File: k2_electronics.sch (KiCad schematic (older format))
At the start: 60 parts, among them J1 Conn_ARM_JTAG_SWD_10, SW1 SW_SPST, SW10 SW_SPST, SW11 SW_SPST, SW12 SW_SPST, SW13 SW_SPST, SW14 SW_SPST, SW15 SW_SPST, SW16 SW_SPST, SW17 SW_SPST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

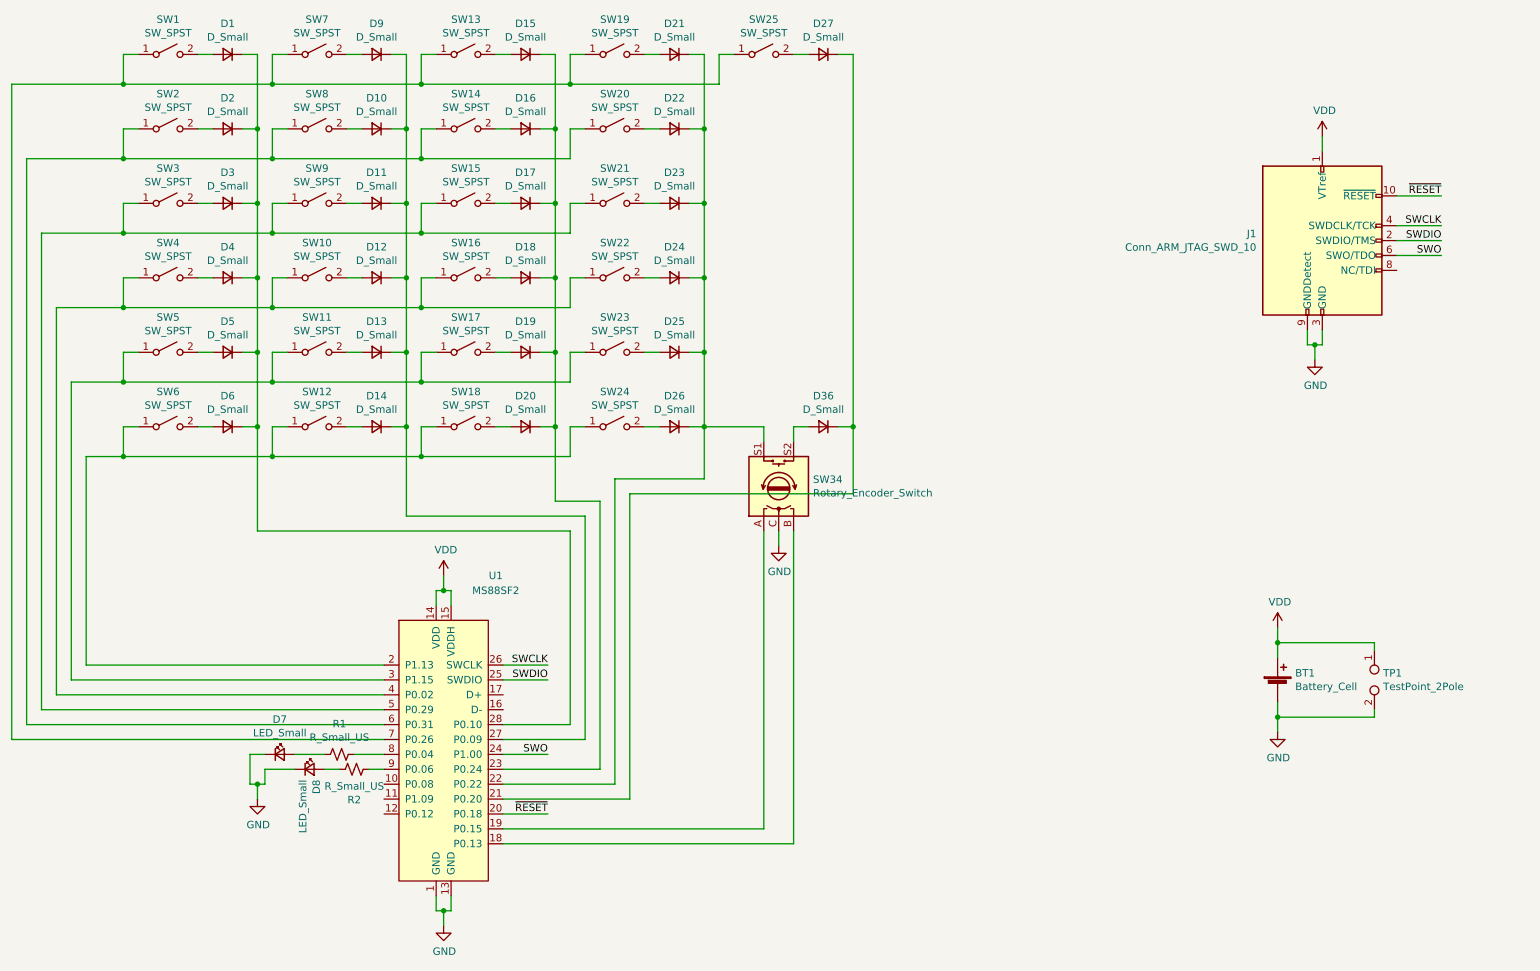
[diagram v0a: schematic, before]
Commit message: Component placement and autoroute
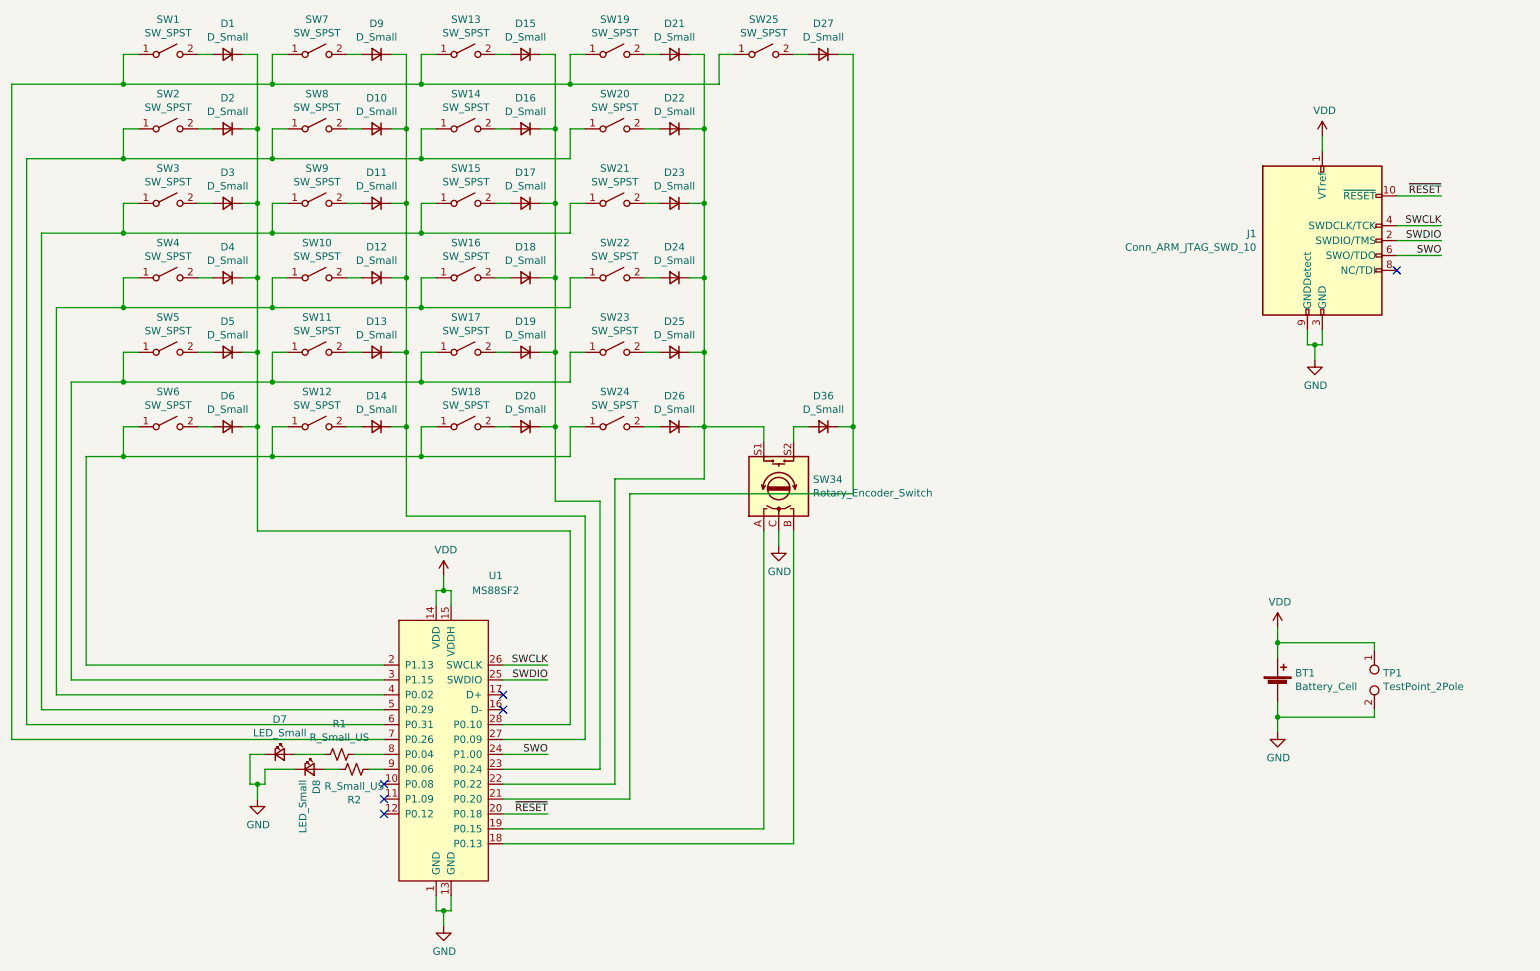
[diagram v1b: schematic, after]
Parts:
- D7, D8: footprint LED_SMD:LED_0603_1608Metric_Pad1.05x0.95mm_HandSolder -> k2:LED_0603_1608Metric_Pad1.05x0.95mm_HandSolder_reversible
- J1: footprint (none) -> Connector_PinHeader_1.27mm:PinHeader_2x05_P1.27mm_Vertical
- R1, R2: footprint Resistor_SMD:R_0603_1608Metric_Pad0.98x0.95mm_HandSolder -> k2:R_0603_1608Metric_Pad0.98x0.95mm_HandSolder_reversible
- TP1: footprint TestPoint:TestPoint_2Pads_Pitch5.08mm_Drill1.3mm -> TestPoint:TestPoint_2Pads_Pitch2.54mm_Drill0.8mm
- U1: footprint (none) -> k2:MS88F2_reversible
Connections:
- no-connect marks 0 -> 6
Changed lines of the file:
@@
 F 0 "U1" H 4150 6650 50  0000 C CNN
 F 1 "MS88SF2" H 4150 6550 50  0000 C CNN
-F 2 "" H 3800 6900 50  0001 C CNN
+F 2 "k2:MS88F2_reversible" H 3800 6900 50  0001 C CNN
 F 3 "" H 3800 6900 50  0001 C CNN
 	1    3800 5600
@@
 F 0 "D8" V 2946 5780 50  0000 R CNN
 F 1 "LED_Small" V 2855 5780 50  0000 R CNN
-F 2 "LED_SMD:LED_0603_1608Metric_Pad1.05x0.95mm_HandSolder" V 2900 5850 50  0001 C CNN
+F 2 "k2:LED_0603_1608Metric_Pad1.05x0.95mm_HandSolder_reversible" V 2900 5850 50  0001 C CNN
 F 3 "~" V 2900 5850 50  0001 C CNN
 	1    2900 5850
@@
 F 0 "D7" H 2700 5985 50  0000 C CNN
 F 1 "LED_Small" H 2700 5894 50  0000 C CNN
-F 2 "LED_SMD:LED_0603_1608Metric_Pad1.05x0.95mm_HandSolder" V 2700 5750 50  0001 C CNN
+F 2 "k2:LED_0603_1608Metric_Pad1.05x0.95mm_HandSolder_reversible" V 2700 5750 50  0001 C CNN
 F 3 "~" V 2700 5750 50  0001 C CNN
 	1    2700 5750
@@
 F 0 "R1" V 3305 5750 50  0000 C CNN
 F 1 "R_Small_US" V 3214 5750 50  0000 C CNN
-F 2 "Resistor_SMD:R_0603_1608Metric_Pad0.98x0.95mm_HandSolder" H 3100 5750 50  0001 C CNN
+F 2 "k2:R_0603_1608Metric_Pad0.98x0.95mm_HandSolder_reversible" H 3100 5750 50  0001 C CNN
 F 3 "~" H 3100 5750 50  0001 C CNN
 	1    3100 5750
@@
 F 0 "R2" V 3405 5850 50  0000 C CNN
 F 1 "R_Small_US" V 3314 5850 50  0000 C CNN
-F 2 "Resistor_SMD:R_0603_1608Metric_Pad0.98x0.95mm_HandSolder" H 3200 5850 50  0001 C CNN
+F 2 "k2:R_0603_1608Metric_Pad0.98x0.95mm_HandSolder_reversible" H 3200 5850 50  0001 C CNN
 F 3 "~" H 3200 5850 50  0001 C CNN
 	1    3200 5850
@@
 F 0 "J1" H 9257 2346 50  0000 R CNN
 F 1 "Conn_ARM_JTAG_SWD_10" H 9257 2255 50  0000 R CNN
-F 2 "" H 9700 2300 50  0001 C CNN
+F 2 "Connector_PinHeader_1.27mm:PinHeader_2x05_P1.27mm_Vertical" H 9700 2300 50  0001 C CNN
 F 3 "http://infocenter.arm.com/help/topic/com.arm.doc.ddi0314h/DDI0314H_coresight_components_trm.pdf" V 9350 1050 50  0001 C CNN
 	1    9700 2300
@@
 F 0 "TP1" V 10004 5308 50  0000 L CNN
 F 1 "TestPoint_2Pole" V 10095 5308 50  0000 L CNN
-F 2 "TestPoint:TestPoint_2Pads_Pitch5.08mm_Drill1.3mm" H 10050 5250 50  0001 C CNN
+F 2 "TestPoint:TestPoint_2Pads_Pitch2.54mm_Drill0.8mm" H 10050 5250 50  0001 C CNN
 F 3 "~" H 10050 5250 50  0001 C CNN
 	1    10050 5250
@@
 Wire Wire Line
 	6150 6350 6150 4250
+NoConn ~ 10200 2500
+NoConn ~ 3400 5950
+NoConn ~ 3400 6050
+NoConn ~ 3400 6150
+NoConn ~ 4200 5350
+NoConn ~ 4200 5450
 $EndSCHEMATC

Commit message: Ensure all footprints reversible and touchup
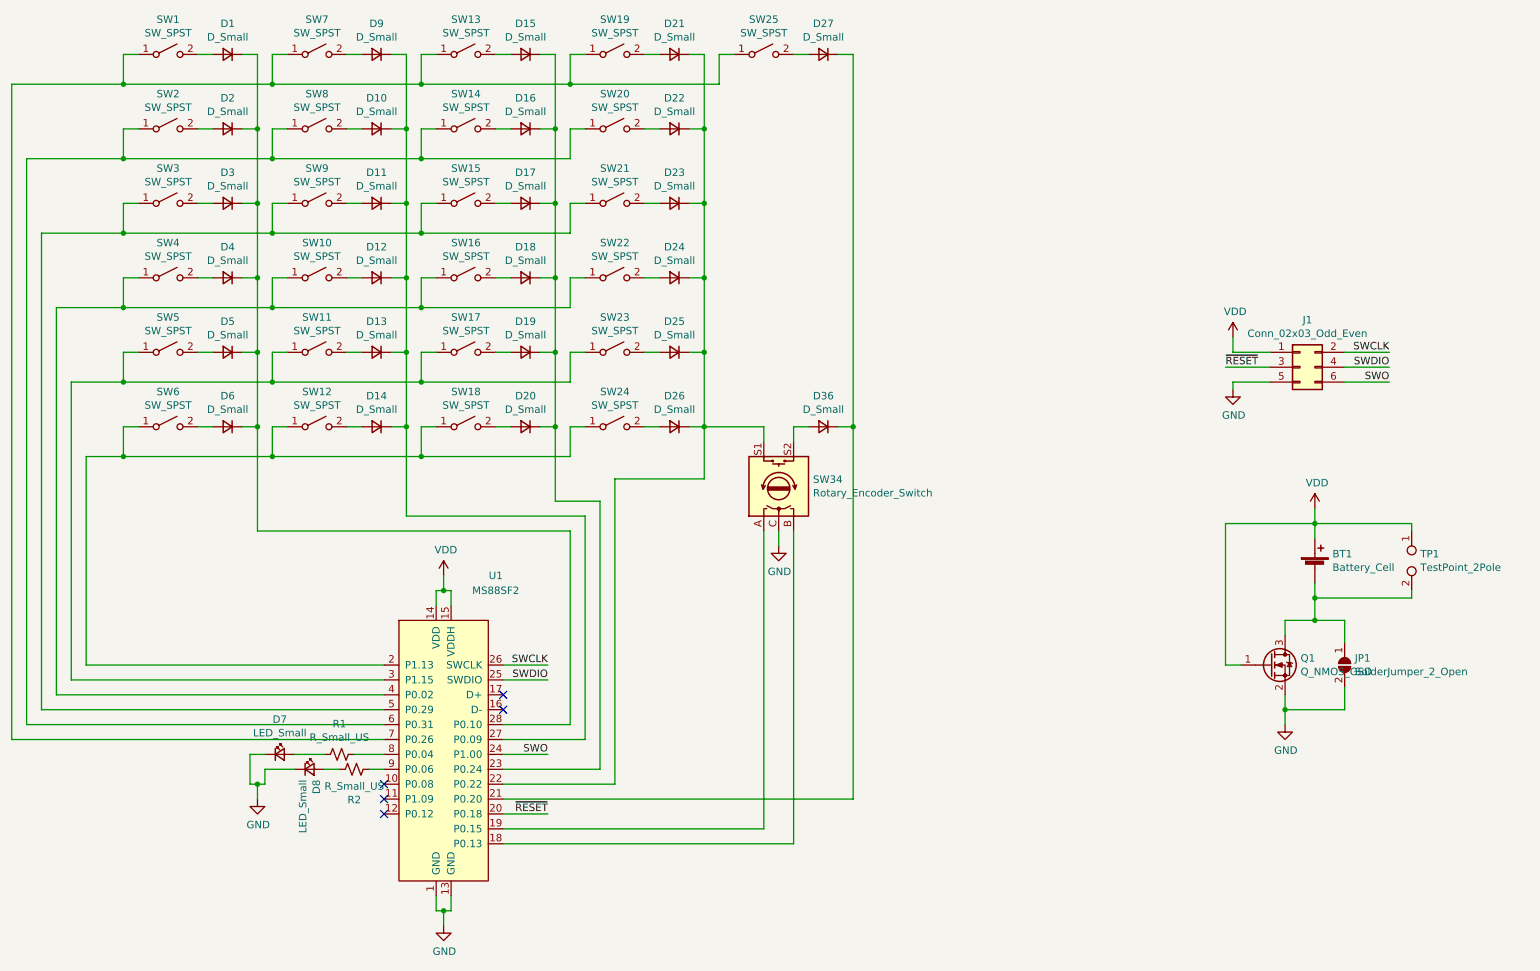
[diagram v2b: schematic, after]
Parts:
- removed J1: Conn_ARM_JTAG_SWD_10, Connector_PinHeader_1.27mm:PinHeader_2x05_P1.27mm_Vertical, symbol Connector:Conn_ARM_JTAG_SWD_10
- added J1: Conn_02x03_Odd_Even, Connector_PinHeader_2.54mm:PinHeader_2x03_P2.54mm_Vertical, symbol Connector_Generic:Conn_02x03_Odd_Even
- added JP1: SolderJumper_2_Open, k2:SolderJumper-2_P1.3mm_Open_Pad1.0x1.5mm_reversible, symbol Jumper:SolderJumper_2_Open
- added Q1: Q_NMOS_GSD, k2:SOT-23_Handsoldering_reversible, symbol Device:Q_NMOS_GSD
- BT1: footprint Battery:BatteryHolder_Keystone_3009_1x2450 -> k2:BatteryHolder_Keystone_3009_1x2450_reversible
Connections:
- net GND: now also J1.5 (Pin_5), JP1.2 (B), Q1.2 (S); no longer BT1.2 (-), TP1.2
- net SWCLK: now also J1.2 (Pin_2)
- net SWDIO: now also J1.4 (Pin_4)
- net SWO: now also J1.6 (Pin_6)
- net VDD: now also J1.1 (Pin_1), Q1.1 (G)
- net ~RESET: now also J1.3 (Pin_3)
- new net: BT1.2 (-), JP1.1 (A), Q1.3 (D), TP1.2
- no-connect marks 6 -> 5
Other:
- moved on the sheet: BT1, TP1
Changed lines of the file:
@@
 Wire Wire Line
 	4500 6150 4200 6150
-$Comp
-L Connector:Conn_ARM_JTAG_SWD_10 J1
-U 1 1 60AE0FF7
-P 9700 2300
-F 0 "J1" H 9257 2346 50  0000 R CNN
-F 1 "Conn_ARM_JTAG_SWD_10" H 9257 2255 50  0000 R CNN
-F 2 "Connector_PinHeader_1.27mm:PinHeader_2x05_P1.27mm_Vertical" H 9700 2300 50  0001 C CNN
-F 3 "http://infocenter.arm.com/help/topic/com.arm.doc.ddi0314h/DDI0314H_coresight_components_trm.pdf" V 9350 1050 50  0001 C CNN
-	1    9700 2300
-	1    0    0    -1
-$EndComp
-Text Label 10500 2000 2    50   ~ 0
+Text Label 9050 3150 0    50   ~ 0
 ~RESET
 Wire Wire Line
-	10500 2000 10200 2000
-Text Label 10500 2200 2    50   ~ 0
+	9050 3150 9350 3150
+Text Label 10150 3050 2    50   ~ 0
 SWCLK
-Text Label 10500 2300 2    50   ~ 0
+Text Label 10150 3150 2    50   ~ 0
 SWDIO
 Wire Wire Line
-	10500 2200 10200 2200
-Wire Wire Line
-	10500 2300 10200 2300
+	10150 3050 9850 3050
+Wire Wire Line
+	10150 3150 9850 3150
 Text Label 4500 5750 2    50   ~ 0
 SWO
 Wire Wire Line
 	4200 5750 4500 5750
-Text Label 10500 2400 2    50   ~ 0
+Text Label 10150 3250 2    50   ~ 0
 SWO
 Wire Wire Line
-	10200 2400 10500 2400
+	9850 3250 10150 3250
 $Comp
 L power:GND #PWR0105
 U 1 1 60C0DCCD
-P 9650 3100
-F 0 "#PWR0105" H 9650 2850 50  0001 C CNN
-F 1 "GND" H 9655 2927 50  0000 C CNN
-F 2 "" H 9650 3100 50  0001 C CNN
-F 3 "" H 9650 3100 50  0001 C CNN
-	1    9650 3100
-	1    0    0    -1
-$EndComp
-Wire Wire Line
-	9600 2900 9600 3000
-Wire Wire Line
-	9700 2900 9700 3000
-Wire Wire Line
-	9600 3000 9650 3000
-Wire Wire Line
-	9650 3000 9650 3100
-Connection ~ 9650 3000
-Wire Wire Line
-	9650 3000 9700 3000
-Wire Wire Line
-	9700 1700 9700 1600
+P 9100 3300
+F 0 "#PWR0105" H 9100 3050 50  0001 C CNN
+F 1 "GND" H 9105 3127 50  0000 C CNN
+F 2 "" H 9100 3300 50  0001 C CNN
+F 3 "" H 9100 3300 50  0001 C CNN
+	1    9100 3300
+	1    0    0    -1
+$EndComp
 $Comp
 L power:VDD #PWR0106
 U 1 1 60C1BBFE
-P 9700 1600
-F 0 "#PWR0106" H 9700 1450 50  0001 C CNN
-F 1 "VDD" H 9715 1773 50  0000 C CNN
-F 2 "" H 9700 1600 50  0001 C CNN
-F 3 "" H 9700 1600 50  0001 C CNN
-	1    9700 1600
+P 9100 2950
+F 0 "#PWR0106" H 9100 2800 50  0001 C CNN
+F 1 "VDD" H 9115 3123 50  0000 C CNN
+F 2 "" H 9100 2950 50  0001 C CNN
+F 3 "" H 9100 2950 50  0001 C CNN
+	1    9100 2950
 	1    0    0    -1
 $EndComp
@@
 	5550 3900 5550 3550
 Connection ~ 5550 3550
-Wire Wire Line
-	6550 3550 6550 4000
-Wire Wire Line
-	6550 4000 5050 4000
-Wire Wire Line
-	5050 4000 5050 6050
-Wire Wire Line
-	5050 6050 4200 6050
-$Comp
-L Device:Battery_Cell BT1
-U 1 1 60D64A98
-P 9400 5300
-F 0 "BT1" H 9518 5396 50  0000 L CNN
-F 1 "Battery_Cell" H 9518 5305 50  0000 L CNN
-F 2 "Battery:BatteryHolder_Keystone_3009_1x2450" V 9400 5360 50  0001 C CNN
-F 3 "~" V 9400 5360 50  0001 C CNN
-	1    9400 5300
-	1    0    0    -1
-$EndComp
 $Comp
 L power:VDD #PWR0107
 U 1 1 60D67DA9
-P 9400 4900
-F 0 "#PWR0107" H 9400 4750 50  0001 C CNN
-F 1 "VDD" H 9415 5073 50  0000 C CNN
-F 2 "" H 9400 4900 50  0001 C CNN
-F 3 "" H 9400 4900 50  0001 C CNN
-	1    9400 4900
+P 9650 4100
+F 0 "#PWR0107" H 9650 3950 50  0001 C CNN
+F 1 "VDD" H 9665 4273 50  0000 C CNN
+F 2 "" H 9650 4100 50  0001 C CNN
+F 3 "" H 9650 4100 50  0001 C CNN
+	1    9650 4100
 	1    0    0    -1
 $EndComp
@@
 L power:GND #PWR0108
 U 1 1 60D69398
-P 9400 5600
-F 0 "#PWR0108" H 9400 5350 50  0001 C CNN
-F 1 "GND" H 9405 5427 50  0000 C CNN
-F 2 "" H 9400 5600 50  0001 C CNN
-F 3 "" H 9400 5600 50  0001 C CNN
-	1    9400 5600
-	1    0    0    -1
-$EndComp
-Wire Wire Line
-	9400 5000 9400 5100
-Wire Wire Line
-	9400 5400 9400 5500
-$Comp
-L Connector:TestPoint_2Pole TP1
-U 1 1 60DC161D
-P 10050 5250
-F 0 "TP1" V 10004 5308 50  0000 L CNN
-F 1 "TestPoint_2Pole" V 10095 5308 50  0000 L CNN
-F 2 "TestPoint:TestPoint_2Pads_Pitch2.54mm_Drill0.8mm" H 10050 5250 50  0001 C CNN
-F 3 "~" H 10050 5250 50  0001 C CNN
-	1    10050 5250
-	0    1    1    0
-$EndComp
-Wire Wire Line
-	10050 5050 10050 5000
-Wire Wire Line
-	10050 5000 9400 5000
-Wire Wire Line
-	9400 4900 9400 5000
-Connection ~ 9400 5000
-Wire Wire Line
-	10050 5450 10050 5500
-Wire Wire Line
-	10050 5500 9400 5500
-Wire Wire Line
-	9400 5500 9400 5600
-Connection ~ 9400 5500
+P 9450 5550
+F 0 "#PWR0108" H 9450 5300 50  0001 C CNN
+F 1 "GND" H 9455 5377 50  0000 C CNN
+F 2 "" H 9450 5550 50  0001 C CNN
+F 3 "" H 9450 5550 50  0001 C CNN
+	1    9450 5550
+	1    0    0    -1
+$EndComp
+Wire Wire Line
+	9650 4200 9650 4300
+Wire Wire Line
+	9650 4600 9650 4700
+Wire Wire Line
+	10300 4250 10300 4200
+Wire Wire Line
+	10300 4200 9650 4200
+Wire Wire Line
+	9650 4100 9650 4200
+Connection ~ 9650 4200
+Wire Wire Line
+	10300 4650 10300 4700
+Wire Wire Line
+	10300 4700 9650 4700
 Wire Wire Line
 	6550 1050 6550 3550
@@
 Wire Wire Line
 	6150 6350 6150 4250
-NoConn ~ 10200 2500
 NoConn ~ 3400 5950
 NoConn ~ 3400 6050
@@
 NoConn ~ 4200 5350
 NoConn ~ 4200 5450
+$Comp
+L Connector:TestPoint_2Pole TP1
+U 1 1 60DC161D
+P 10300 4450
+F 0 "TP1" V 10254 4508 50  0000 L CNN
+F 1 "TestPoint_2Pole" V 10345 4508 50  0000 L CNN
+F 2 "TestPoint:TestPoint_2Pads_Pitch2.54mm_Drill0.8mm" H 10300 4450 50  0001 C CNN
+F 3 "~" H 10300 4450 50  0001 C CNN
+	1    10300 4450
+	0    1    1    0
+$EndComp
+$Comp
+L Device:Battery_Cell BT1
+U 1 1 60D64A98
+P 9650 4500
+F 0 "BT1" H 9768 4596 50  0000 L CNN
+F 1 "Battery_Cell" H 9768 4505 50  0000 L CNN
+F 2 "k2:BatteryHolder_Keystone_3009_1x2450_reversible" V 9650 4560 50  0001 C CNN
+F 3 "~" V 9650 4560 50  0001 C CNN
+	1    9650 4500
+	1    0    0    -1
+$EndComp
+$Comp
+L Jumper:SolderJumper_2_Open JP1
+U 1 1 603F95E5
+P 9850 5150
+F 0 "JP1" V 9804 5218 50  0000 L CNN
+F 1 "SolderJumper_2_Open" V 9895 5218 50  0000 L CNN
+F 2 "k2:SolderJumper-2_P1.3mm_Open_Pad1.0x1.5mm_reversible" H 9850 5150 50  0001 C CNN
+F 3 "~" H 9850 5150 50  0001 C CNN
+	1    9850 5150
+	0    1    1    0
+$EndComp
+Wire Wire Line
+	9850 5000 9850 4850
+Wire Wire Line
+	9850 4850 9650 4850
+Wire Wire Line
+	9650 4850 9650 4700
+Connection ~ 9650 4700
+Wire Wire Line
+	9450 4950 9450 4850
+Wire Wire Line
+	9450 4850 9650 4850
+Connection ~ 9650 4850
+Wire Wire Line
+	9850 5450 9450 5450
+Wire Wire Line
+	9450 5450 9450 5550
+Connection ~ 9450 5450
+Wire Wire Line
+	9150 5150 9050 5150
+Wire Wire Line
+	9050 5150 9050 4200
+Wire Wire Line
+	9050 4200 9650 4200
+Wire Wire Line
+	9850 5300 9850 5450
+Wire Wire Line
+	9450 5350 9450 5450
+$Comp
+L Device:Q_NMOS_GSD Q1
+U 1 1 6049FCD3
+P 9350 5150
+F 0 "Q1" H 9554 5196 50  0000 L CNN
+F 1 "Q_NMOS_GSD" H 9554 5105 50  0000 L CNN
+F 2 "k2:SOT-23_Handsoldering_reversible" H 9550 5250 50  0001 C CNN
+F 3 "~" H 9350 5150 50  0001 C CNN
+	1    9350 5150
+	1    0    0    -1
+$EndComp
+$Comp
+L Connector_Generic:Conn_02x03_Odd_Even J1
+U 1 1 604D509E
+P 9550 3150
+F 0 "J1" H 9600 3467 50  0000 C CNN
+F 1 "Conn_02x03_Odd_Even" H 9600 3376 50  0000 C CNN
+F 2 "Connector_PinHeader_2.54mm:PinHeader_2x03_P2.54mm_Vertical" H 9550 3150 50  0001 C CNN
+F 3 "~" H 9550 3150 50  0001 C CNN
+	1    9550 3150
+	1    0    0    -1
+$EndComp
+Wire Wire Line
+	9100 2950 9100 3050
+Wire Wire Line
+	9100 3050 9350 3050
+Wire Wire Line
+	9100 3300 9100 3250
+Wire Wire Line
+	9100 3250 9350 3250
+Wire Wire Line
+	6550 3550 6550 6050
+Wire Wire Line
+	4200 6050 6550 6050
 $EndSCHEMATC
